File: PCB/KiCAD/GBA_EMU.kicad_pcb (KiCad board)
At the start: 2 copper layers, 130.7 x 72.9 mm, 14 parts

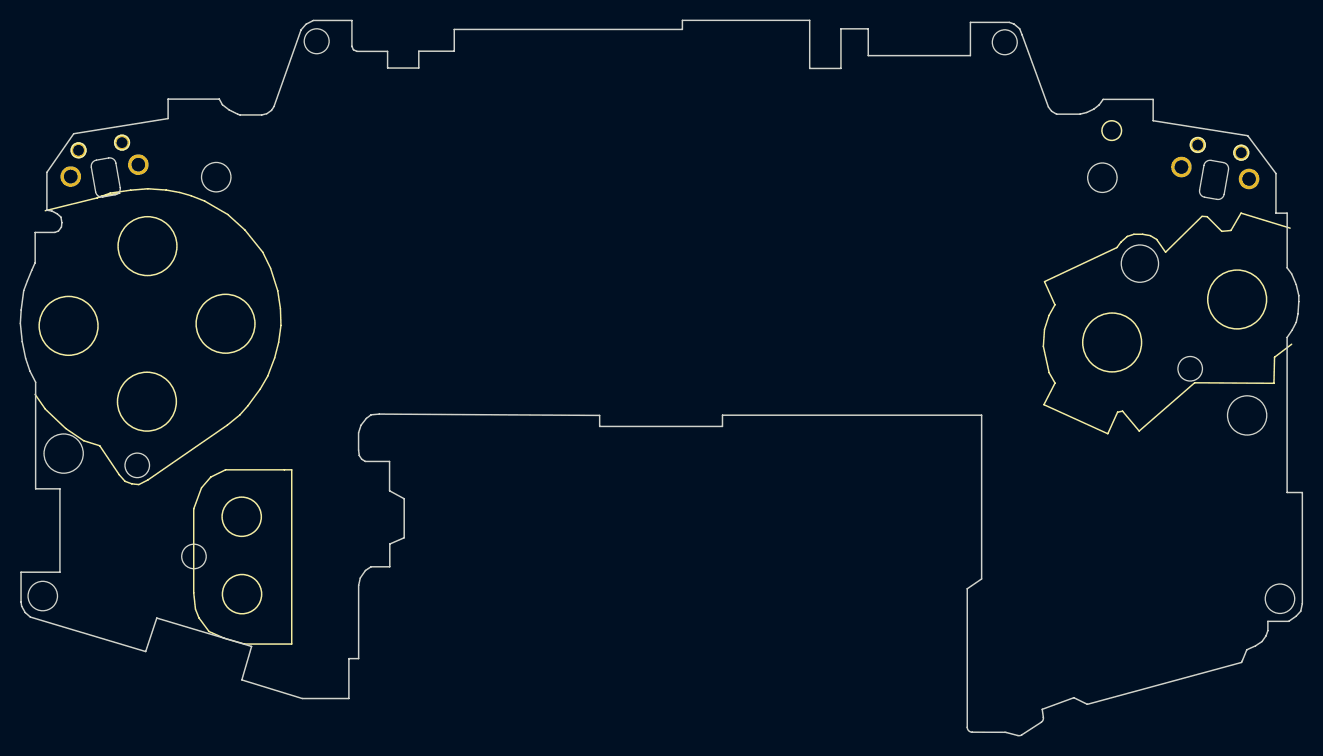
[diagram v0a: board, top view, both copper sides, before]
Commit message: imported footprints
button footprints from https://github.com/AEFeinstein/gbaZero
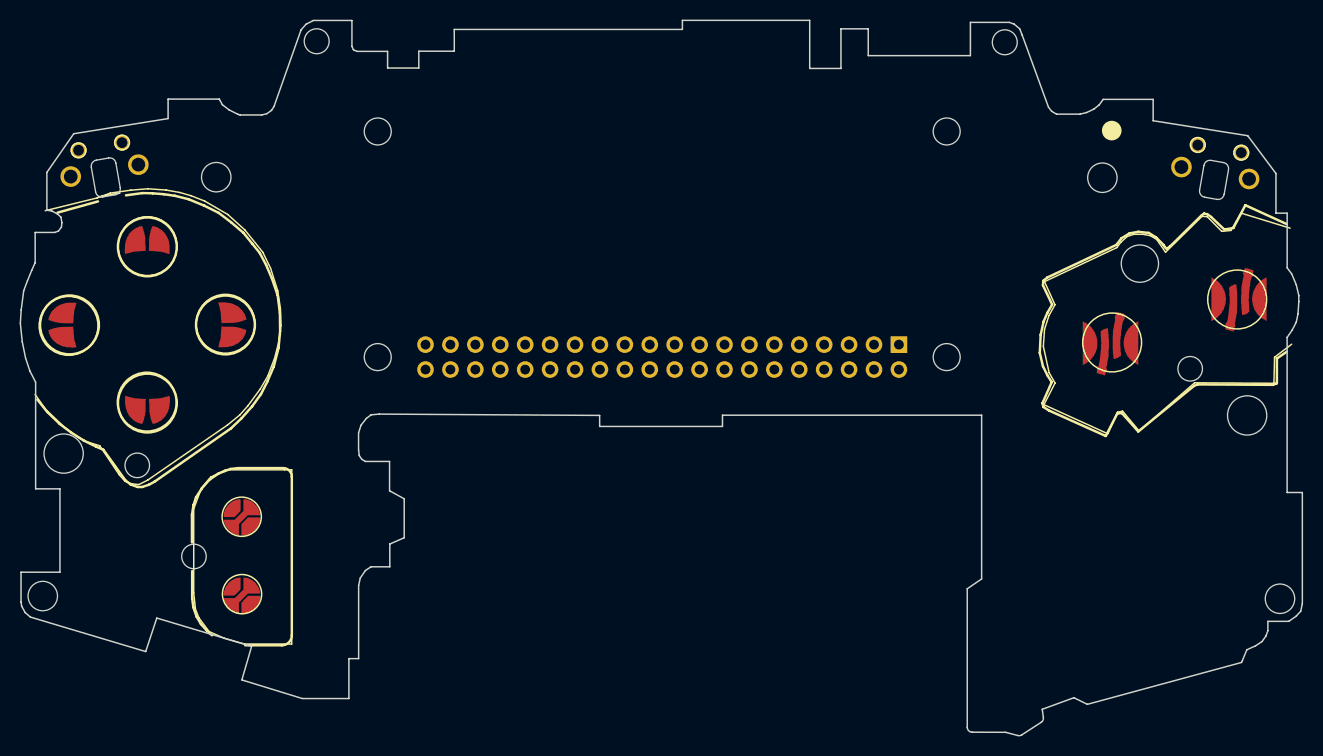
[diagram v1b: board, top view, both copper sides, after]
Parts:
- removed S1, S2: SHOULDER_BUTTON, GBA_EMU:SHOULDER_BUTTON
- added J1: Raspberry_Pi_2_3, Module:Raspberry_Pi_Zero_Socketed_THT_FaceDown_MountingHoles, B.Cu at (172.7, 101.6)
- added SW_AB1: SW_DIP_x02, GBA_EMU:AB_BUTTON, F.Cu at (200.8, 99.2)
- added SW_DPAD1: SW_DIP_x04, GBA_EMU:D-PAD, F.Cu at (96.1, 99.6)
- added SW_L1: SW_DIP_x01, GBA_EMU:SHOULDER_BUTTON, F.Cu at (91.7, 83.9)
- added SW_R1: SW_DIP_x01, GBA_EMU:SHOULDER_BUTTON, B.Cu at (205.0, 84.1)
- added SW_SS1: SW_DIP_x02, GBA_EMU:START_SELECT_BUTTON, F.Cu at (105.8, 123.2)
